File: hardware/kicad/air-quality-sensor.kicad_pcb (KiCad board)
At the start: 2 copper layers, 80 x 90 mm, 9 parts, among them U1 XIAO_ESP32C3, U2 SCD41, U3 SGP41, U4 SSD1306_0.96, U5 TP4056_Module

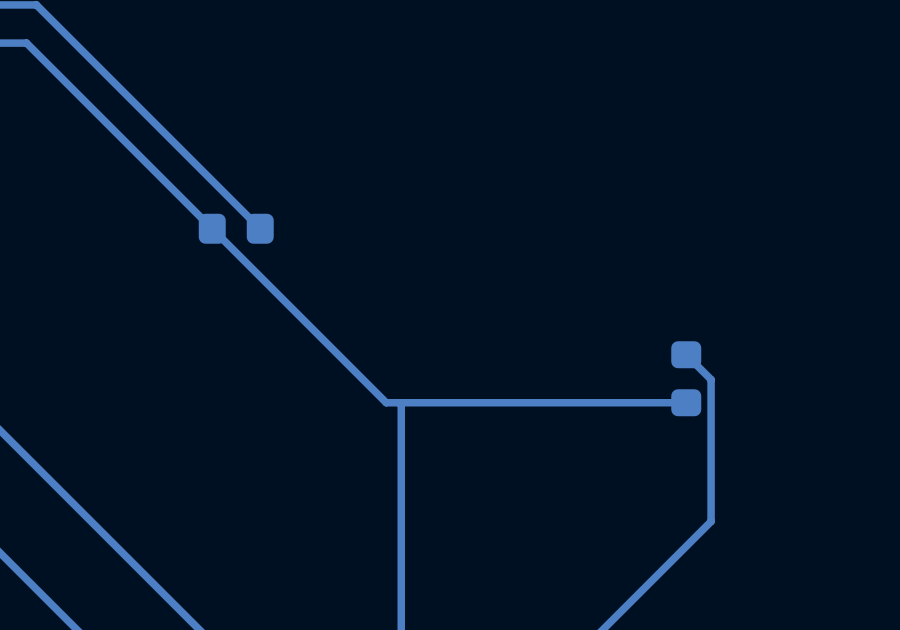
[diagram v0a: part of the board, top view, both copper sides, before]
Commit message: Finalize v3 MCP board respin: PMSA003I PM sensor + 5 V boost power tree
Commit the June 2026 design session that was never landed: U1 switched to a
through-hole DIP footprint, Adafruit PMSA003I (U6) added on the shared I2C
bus, TPS61023-class 5 V boost (U7) + SS14 Schottky (D1) power tree for
battery-only operation. 19 symbols, ERC 0 errors, 160 routed tracks, DRC
clean; manufacturing outputs regenerated. BOARD-DESIGN-NOTES.md records
board-specific status and open items; MCP-FUTURE-CHANGES.md records the
MCP-only workflow policy and validation baseline. Ignore local KiCad/MCP
editor artifacts (prl, validation caches, eval scratch files).
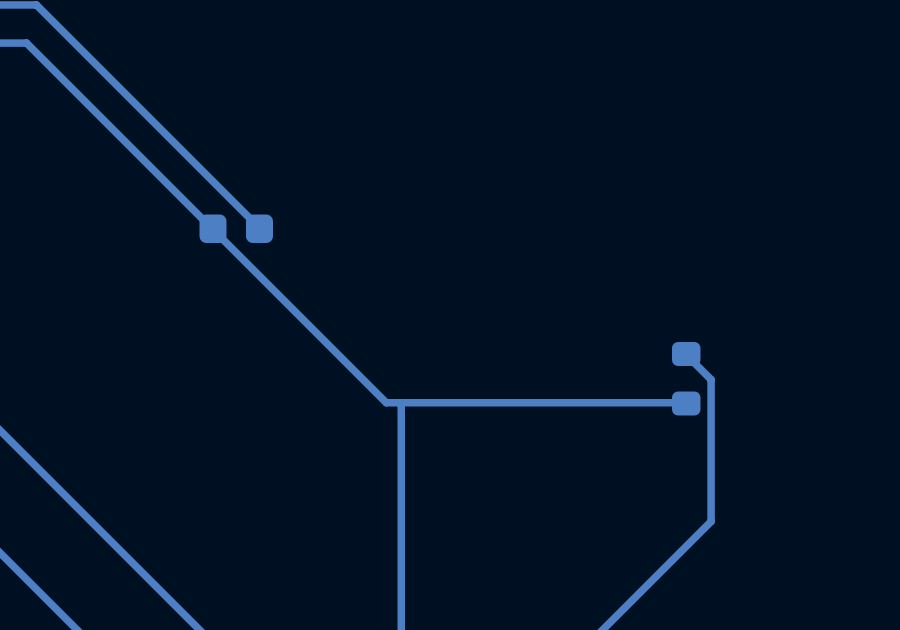
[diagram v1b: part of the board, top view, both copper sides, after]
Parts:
- U1: value XIAO_ESP32C3 -> ESP32C3
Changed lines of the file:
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@@
 			)
 		)
-		(property "Value" "XIAO_ESP32C3"
+		(property "Value" "ESP32C3"
 			(at 0 1 270)
 			(unlocked yes)
@@
 		(layer "B.Cu")
 		(at 150 60 90)
-		(descr "Resistor SMD 0603")
+		(descr "Resistor SMD 0603 (1608 Metric), square (rectangular) end terminal, IPC-7351 nominal, (Body size source: IPC-SM-782 page 72, https://www.pcb-3d.com/wordpress/wp-content/uploads/ipc-sm-782a_amendment_1_and_2.pdf), generated with kicad-footprint-generator")
 		(tags "resistor")
 		(property "Reference" "R1"
@@
 		(attr smd)
 		(fp_line
-			(start -0.8 -0.4)
-			(end 0.8 -0.4)
+			(start -0.237258 -0.5225)
+			(end 0.237258 -0.5225)
+			(stroke
+				(width 0.12)
+				(type solid)
+			)
+			(layer "B.SilkS")
+		)
+		(fp_line
+			(start -0.237258 0.5225)
+			(end 0.237258 0.5225)
+			(stroke
+				(width 0.12)
+				(type solid)
+			)
+			(layer "B.SilkS")
+		)
+		(fp_rect
+			(start -1.48 0.73)
+			(end 1.48 -0.73)
+			(stroke
+				(width 0.05)
+				(type solid)
+			)
+			(fill no)
+			(layer "B.CrtYd")
+		)
+		(fp_rect
+			(start -0.8 0.4125)
+			(end 0.8 -0.4125)
 			(stroke
 				(width 0.1)
 				(type solid)
 			)
-			(layer "B.SilkS")
-		)
-		(fp_line
-			(start -0.8 0.4)
-			(end 0.8 0.4)
-			(stroke
-				(width 0.1)
-				(type solid)
-			)
-			(layer "B.SilkS")
+			(fill no)
+			(layer "B.Fab")
+		)
+		(fp_text user "${REFERENCE}"
+			(at 0 0 270)
+			(layer "B.Fab")
+			(effects
+				(font
+					(size 0.4 0.4)
+					(thickness 0.06)
+				)
+				(justify mirror)
+			)
 		)
 		(pad "1" smd roundrect
-			(at -0.8 0 90)
-			(size 0.9 1)
+			(at -0.825 0 90)
+			(size 0.8 0.95)
 			(layers "B.Cu" "B.Mask" "B.Paste")
 			(roundrect_rratio 0.25)
@@
 		)
 		(pad "2" smd roundrect
-			(at 0.8 0 90)
-			(size 0.9 1)
+			(at 0.825 0 90)
+			(size 0.8 0.95)
 			(layers "B.Cu" "B.Mask" "B.Paste")
 			(roundrect_rratio 0.25)
@@
 		)
 		(embedded_fonts no)
+		(model "${KICAD9_3DMODEL_DIR}/Resistor_SMD.3dshapes/R_0603_1608Metric.step"
+			(offset
+				(xyz 0 0 0)
+			)
+			(scale
+				(xyz 1 1 1)
+			)
+			(rotate
+				(xyz 0 0 0)
+			)
+		)
 	)
 	(footprint "Capacitor_SMD:C_0603_1608Metric"
 		(layer "B.Cu")
 		(at 135 55)
-		(descr "Capacitor SMD 0603")
+		(descr "Capacitor SMD 0603 (1608 Metric), square (rectangular) end terminal, IPC-7351 nominal, (Body size source: IPC-SM-782 page 76, https://www.pcb-3d.com/wordpress/wp-content/uploads/ipc-sm-782a_amendment_1_and_2.pdf), generated with kicad-footprint-generator")
 		(tags "capacitor")
 		(property "Reference" "C1"
@@
 		(sheetfile "air-quality-sensor.kicad_sch")
 		(attr smd)
+		(fp_line
+			(start -0.14058 -0.51)
+			(end 0.14058 -0.51)
+			(stroke
+				(width 0.12)
+				(type solid)
+			)
+			(layer "B.SilkS")
+		)
+		(fp_line
+			(start -0.14058 0.51)
+			(end 0.14058 0.51)
+			(stroke
+				(width 0.12)
+				(type solid)
+			)
+			(layer "B.SilkS")
+		)
+		(fp_rect
+			(start -1.48 0.73)
+			(end 1.48 -0.73)
+			(stroke
+				(width 0.05)
+				(type solid)
+			)
+			(fill no)
+			(layer "B.CrtYd")
+		)
+		(fp_rect
+			(start -0.8 0.4)
+			(end 0.8 -0.4)
+			(stroke
+				(width 0.1)
+				(type solid)
+			)
+			(fill no)
+			(layer "B.Fab")
+		)
+		(fp_text user "${REFERENCE}"
+			(at 0 0 180)
+			(layer "B.Fab")
+			(effects
+				(font
+					(size 0.4 0.4)
+					(thickness 0.06)
+				)
+				(justify mirror)
+			)
+		)
 		(pad "1" smd roundrect
-			(at -0.8 0)
-			(size 0.9 1)
+			(at -0.775 0)
+			(size 0.9 0.95)
 			(layers "B.Cu" "B.Mask" "B.Paste")
 			(roundrect_rratio 0.25)
@@
 		)
 		(pad "2" smd roundrect
-			(at 0.8 0)
-			(size 0.9 1)
+			(at 0.775 0)
+			(size 0.9 0.95)
 			(layers "B.Cu" "B.Mask" "B.Paste")
 			(roundrect_rratio 0.25)
@@
 		)
 		(embedded_fonts no)
+		(model "${KICAD9_3DMODEL_DIR}/Capacitor_SMD.3dshapes/C_0603_1608Metric.step"
+			(offset
+				(xyz 0 0 0)
+			)
+			(scale
+				(xyz 1 1 1)
+			)
+			(rotate
+				(xyz 0 0 0)
+			)
+		)
 	)
 	(gr_line
